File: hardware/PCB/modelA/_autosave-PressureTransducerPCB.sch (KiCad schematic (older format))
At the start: 24 parts, among them J1 Conn_01x05_Male, J2 MS5803_HDR, J3 JST_PowerPlug, J4 Micro_SD, U1 ATmega328PB-AU, U2 DS3231SN, U3 TPS7A0333PDBVR

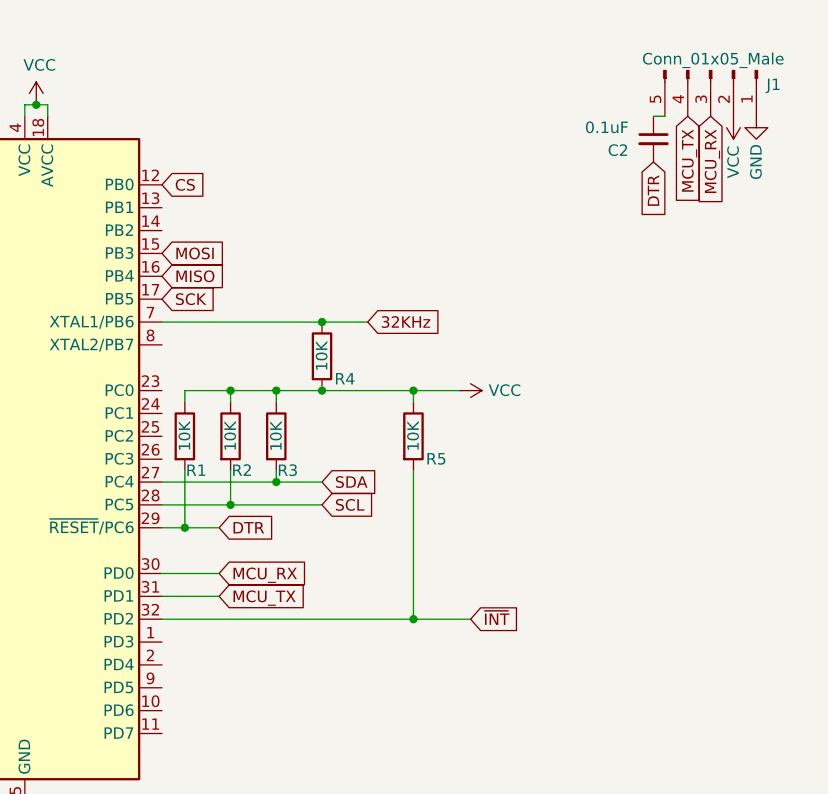
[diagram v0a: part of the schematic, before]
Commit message: Finish first layout design with minor schematic changes
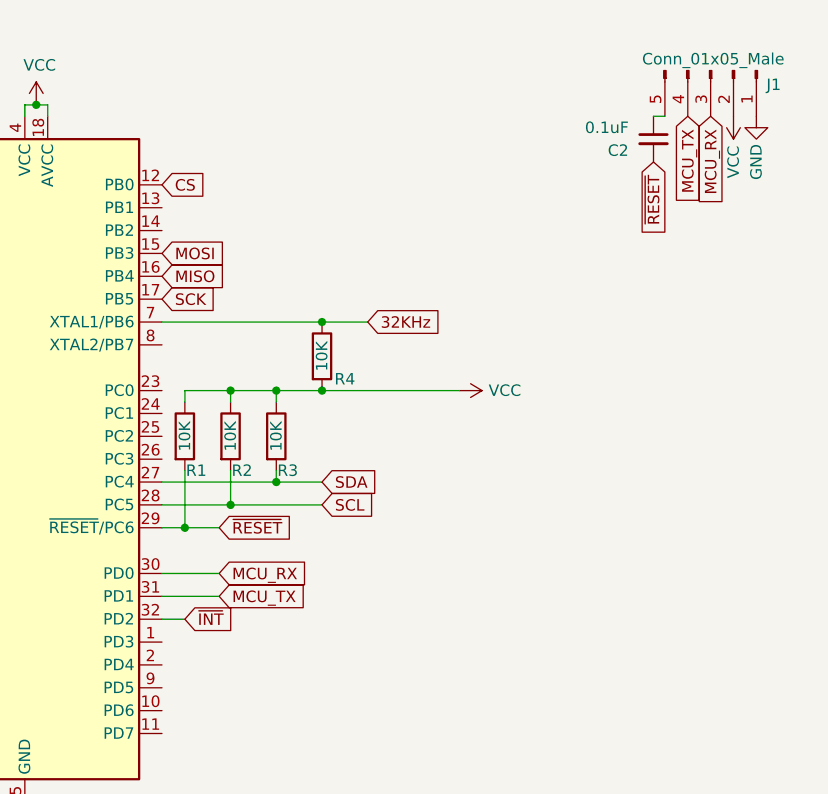
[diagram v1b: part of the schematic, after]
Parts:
- removed R5: 10K, Resistor_SMD:R_0805_2012Metric, symbol Device:R
- C1, C2, C3, C4: footprint Capacitor_SMD:C_0805_2012Metric -> Capacitor_SMD:C_0402_1005Metric
- J2: footprint Connector_JST:JST_PH_S5B-PH-K_1x05_P2.00mm_Horizontal -> Connector_JST:JST_PH_S4B-PH-K_1x04_P2.00mm_Horizontal
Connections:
- net DTR renamed ~RESET
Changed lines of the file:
@@
 F 0 "C4" V 8700 1050 50  0000 L CNN
 F 1 "0.1uF" V 8500 1050 50  0000 L CNN
-F 2 "Capacitor_SMD:C_0805_2012Metric" H 8688 1050 50  0001 C CNN
+F 2 "Capacitor_SMD:C_0402_1005Metric" H 8688 1050 50  0001 C CNN
 F 3 "~" H 8650 1200 50  0001 C CNN
 	1    8650 1200
@@
 F 0 "C1" H 1100 1050 50  0000 L CNN
 F 1 "0.1uF" H 1100 1150 50  0000 L CNN
-F 2 "Capacitor_SMD:C_0805_2012Metric" H 1038 950 50  0001 C CNN
+F 2 "Capacitor_SMD:C_0402_1005Metric" H 1038 950 50  0001 C CNN
 F 3 "~" H 1000 1100 50  0001 C CNN
 	1    1000 1100
@@
 Text GLabel 9400 1900 2    50   Input ~ 0
 ~INT
-Text GLabel 4550 3200 2    50   Input ~ 0
+Text GLabel 3300 3200 2    50   Input ~ 0
 ~INT
 Connection ~ 3900 1900
@@
 F 0 "C3" H 8300 4100 50  0000 L CNN
 F 1 "0.1uF" H 8200 4200 50  0000 L CNN
-F 2 "Capacitor_SMD:C_0805_2012Metric" H 8500 4150 50  0001 C CNN
+F 2 "Capacitor_SMD:C_0402_1005Metric" H 8500 4150 50  0001 C CNN
 F 3 "~" H 8500 4150 50  0001 C CNN
 	1    8500 4150
@@
 F 0 "J2" V 6600 1000 50  0000 C CNN
 F 1 "MS5803_HDR" V 6500 750 50  0000 C CNN
-F 2 "Connector_JST:JST_PH_S5B-PH-K_1x05_P2.00mm_Horizontal" H 6550 800 50  0001 C CNN
+F 2 "Connector_JST:JST_PH_S4B-PH-K_1x04_P2.00mm_Horizontal" H 6550 800 50  0001 C CNN
 F 3 "~" H 6550 800 50  0001 C CNN
 	1    6550 800
@@
 F 3 "" H 6650 1000 50  0001 C CNN
 	1    6650 1000
-	1    0    0    -1
-$EndComp
-Wire Wire Line
-	4300 3200 4550 3200
-Connection ~ 4300 3200
-Wire Wire Line
-	4300 2200 4500 2200
-Connection ~ 4300 2200
-Wire Wire Line
-	3200 3200 4300 3200
-Wire Wire Line
-	3900 2200 4300 2200
-Wire Wire Line
-	4300 2250 4300 2200
-Wire Wire Line
-	4300 2550 4300 3200
-$Comp
-L Device:R R5
-U 1 1 60B25EED
-P 4300 2400
-F 0 "R5" H 4400 2300 50  0000 C CNN
-F 1 "10K" V 4300 2400 50  0000 C CNN
-F 2 "Resistor_SMD:R_0805_2012Metric" V 4230 2400 50  0001 C CNN
-F 3 "~" H 4300 2400 50  0001 C CNN
-	1    4300 2400
 	1    0    0    -1
 $EndComp
@@
 Text GLabel 5500 1000 3    50   Input ~ 0
 MCU_TX
-Text GLabel 5350 1200 3    50   Input ~ 0
-DTR
 $Comp
 L Device:C_Small C2
@@
 F 0 "C2" H 5150 1050 50  0000 L CNN
 F 1 "0.1uF" H 5050 1150 50  0000 L CNN
-F 2 "Capacitor_SMD:C_0805_2012Metric" H 5350 1100 50  0001 C CNN
+F 2 "Capacitor_SMD:C_0402_1005Metric" H 5350 1100 50  0001 C CNN
 F 3 "~" H 5350 1100 50  0001 C CNN
 	1    5350 1100
@@
 	5350 1000 5400 1000
 Text GLabel 3450 2800 2    50   Input ~ 0
-DTR
+~RESET
 Wire Wire Line
 	3300 2800 3450 2800
@@
 	0    -1   -1   0
 $EndComp
+Wire Wire Line
+	3900 2200 4500 2200
+Wire Wire Line
+	3200 3200 3300 3200
+Text GLabel 5350 1200 3    50   Input ~ 0
+~RESET
 $EndSCHEMATC
